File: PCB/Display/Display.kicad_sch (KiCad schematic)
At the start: 30 parts, among them J1 DC, J2 USB-C, M1 OLED1.5-RGB, U1 L86-M33, U2 ESP32-PICO-MINI-02, U3 FT231XQ, U4 LMR16006+FB, U5 QR

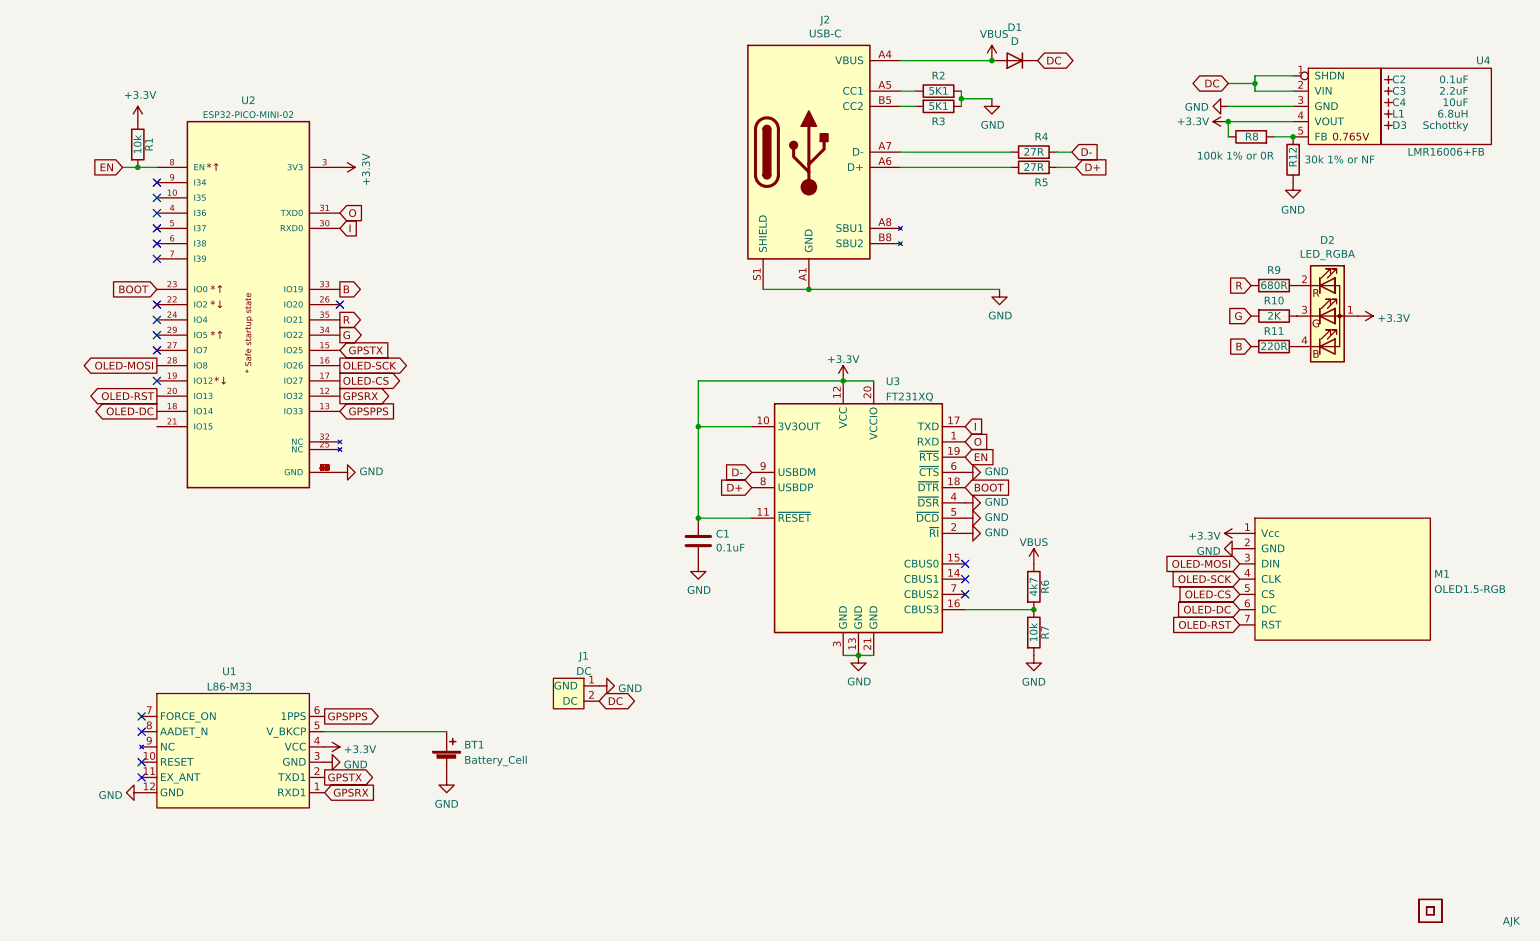
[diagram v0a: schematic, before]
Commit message: Started update on display.
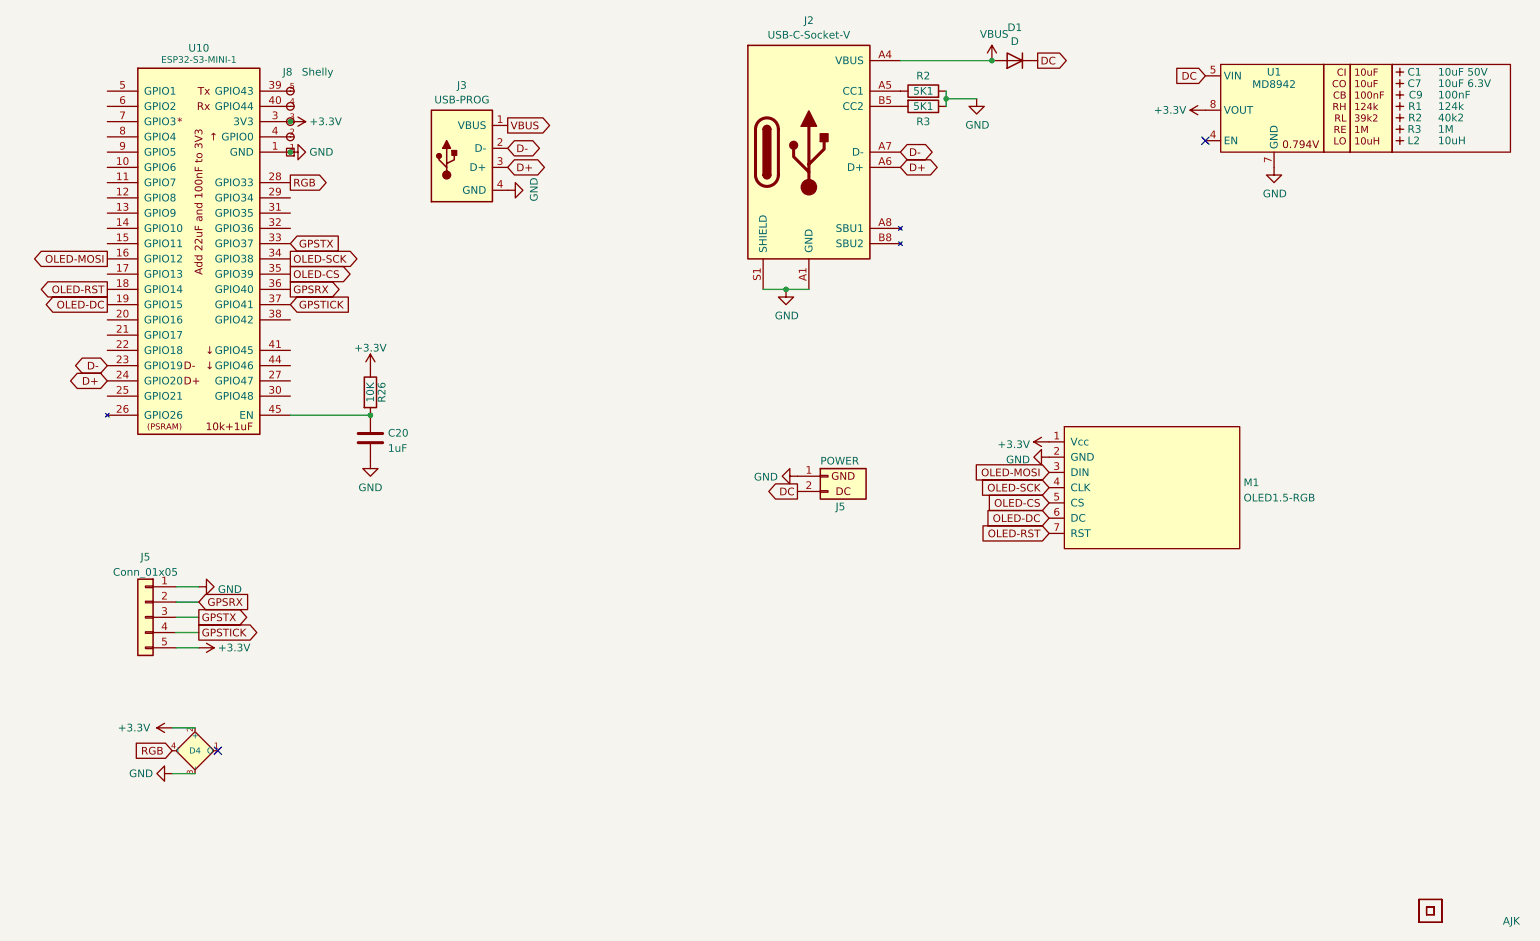
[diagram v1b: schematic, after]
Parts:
- removed BT1: Battery_Cell, RevK:Battery-Holder-2032, symbol Device:Battery_Cell
- removed C1: 0.1uF, RevK:C_0603, symbol Device:C
- removed C2: 0.1uF, RevK:Hidden, symbol RevK:Hidden
- removed C3: 2.2uF, RevK:Hidden, symbol RevK:Hidden
- removed C4: 10uF, RevK:Hidden, symbol RevK:Hidden
- removed D2: LED_RGBA, RevK:LED-RGB-1.6x1.6, symbol Device:LED_ARGB
- removed D3: Schottky, RevK:Hidden, symbol RevK:Hidden
- removed J1: DC, RevK:Molex_MiniSPOX_H2RA, symbol RevK:DC
- removed J2: USB-C, RevK:USC16-TR-Round, symbol RevK:USB-C
- removed L1: 6.8uH, RevK:Hidden, symbol RevK:Hidden
- removed R1, R7: 10k, RevK:R_0603, symbol Device:R
- removed R10: 2K, RevK:R_0603, symbol Device:R
- removed R11: 220R, RevK:R_0603, symbol Device:R
- removed R12: 30k 1% or NF, RevK:R_0603, symbol Device:R
- removed R4, R5: 27R, RevK:R_0603, symbol Device:R
- removed R6: 4k7, RevK:R_0603, symbol Device:R
- removed R8: 100k 1% or 0R, RevK:R_0603, symbol Device:R
- removed R9: 680R, RevK:R_0603, symbol Device:R
- removed U1: L86-M33, RevK:L86-M33, symbol RevK:L86-M33
- removed U2: ESP32-PICO-MINI-02, RevK:ESP32-PICO-MINI-02, symbol RevK:ESP32-PICO-MINI-02
- removed U3: FT231XQ, RevK:QFN-20-1EP_4x4mm_P0.5mm_EP2.5x2.5mm, symbol RevK:FT231XQ
- removed U4: LMR16006+FB, RevK:RegulatorBlockFB, symbol RevK:LMR16006+FB
- added C1: 10uF 50V, RevK:C_0603_, symbol RevK:Hidden
- added C20: 1uF, RevK:C_0402, symbol Device:C
- added C7: 10uF 6.3V, RevK:C_0603_, symbol RevK:Hidden
- added C9: 100nF, RevK:C_0603_, symbol RevK:Hidden
- added D4: XL-1010RGBC-WS2812B, RevK:SMD1010, symbol RevK:WS2812B-1mm
- added J2: USB-C-Socket-V, RevK:USB-C-Socket-H, symbol RevK:USB-C-Socket-H
- added J3: USB-PROG, RevK:USB-PROG, symbol RevK:USB-PROG
- added J5: POWER, RevK:PTSM-HH1-2-RA, symbol RevK:PowerIn
- added J5: Conn_01x05, RevK:PTSM-HH-5-RA-SMD, symbol Connector_Generic:Conn_01x05
- added J8: Shelly, RevK:Shelly, symbol RevK:Shelly
- added L2: 10uH, RevK:L_4x4_, symbol RevK:Hidden
- added R1: 124k, RevK:R_0402_, symbol RevK:Hidden
- added R2: 40k2, RevK:R_0402_, symbol RevK:Hidden
- added R26: 10K, RevK:R_0402, symbol Device:R
- added R3: 1M, RevK:R_0402_, symbol RevK:Hidden
- added U1: MD8942, RevK:SOT-23-6-MD8942, symbol RevK:MD89420-RegBlock
- added U10: ESP32-S3-MINI-1, RevK:ESP32-S3-MINI-1, symbol RevK:ESP32-S3-MINI-1-N4R2
- R2, R3: footprint RevK:R_0603 -> RevK:R_0402
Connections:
- net +3V3: now also D4.2 (+), J5.5 (Pin_5), J8.3 (3V3), R26.1, U1.8 (VOUT), U10.3 (3V3)
- net D+: now also J2.A6 (D+), J2.B6 (D+), J3.3 (D+), U10.24 (GPIO20)
- net D-: now also J2.A7 (D-), J2.B7 (D-), J3.2 (D-), U10.23 (GPIO19)
- net DC: now also J5.2 (DC), U1.5 (VIN)
- net GND: now also C20.2, D4.3 (-), J2.A1 (GND), J2.A12 (GND), J2.B1 (GND), J2.B12 (GND), J2.S1 (SHIELD), J3.4 (GND), J5.1 (GND), J5.1 (Pin_1), J8.1 (GND), U1.2 (GND), U1.7 (GND), U10.1 (GND), U10.2 (GND), U10.42 (GND), U10.43 (GND), U10.46 (GND), U10.47 (GND), U10.48 (GND), U10.49 (GND), U10.50 (GND), U10.51 (GND), U10.52 (GND), U10.53 (GND), U10.54 (GND), U10.55 (GND), U10.56 (GND), U10.57 (GND), U10.58 (GND), U10.59 (GND), U10.60 (GND), U10.61 (GND), U10.62 (GND), U10.63 (GND), U10.64 (GND), U10.65 (GND)
- net GPSRX: now also J5.2 (Pin_2), U10.36 (GPIO40)
- net GPSTX: now also J5.3 (Pin_3), U10.33 (GPIO37)
- net OLED-CS: now also U10.35 (GPIO39)
- net OLED-DC: now also U10.19 (GPIO15)
- net OLED-MOSI: now also U10.16 (GPIO12)
- net OLED-RST: now also U10.18 (GPIO14)
- net OLED-SCK: now also U10.34 (GPIO38)
- net VBUS: now also J2.A4 (VBUS), J2.A9 (VBUS), J2.B4 (VBUS), J2.B9 (VBUS), J3.1 (VBUS)
- net at R2.1: now also J2.A5 (CC1)
- net at R3.2: now also J2.B5 (CC2)
- new net: J8.5 (Tx), U10.39 (GPIO43)
- new net: J8.2 (0), U10.4 (GPIO0)
- new net: J8.4 (Rx), U10.40 (GPIO44)
- new net: C20.1, R26.2, U10.45 (EN)
- new net GPSTICK: J5.4 (Pin_4), U10.37 (GPIO41)
- new net RGB: D4.4 (I), U10.28 (GPIO33)
- no-connect marks 19 -> 2
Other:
- moved on the sheet: M1, R2, R3

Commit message: SD
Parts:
- added J6: DM3AT-SF-PEJM5, Connector_Card:microSD_HC_Hirose_DM3AT-SF-PEJM5, symbol Connector:Micro_SD_Card
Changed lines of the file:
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@@
+    )
+  )
+  (symbol (lib_id "Connector:Micro_SD_Card") (at 143.51 132.715 0) (unit 1)
+    (in_bom yes) (on_board yes) (dnp no) (fields_autoplaced)
+    (property "Reference" "J6" (at 144.145 114.6007 0)
+      (effects (font (size 1.27 1.27)))
+    )
+    (property "Value" "DM3AT-SF-PEJM5" (at 144.145 117.0249 0)
+      (effects (font (size 1.27 1.27)))
+    )
+    (property "Footprint" "Connector_Card:microSD_HC_Hirose_DM3AT-SF-PEJM5" (at 172.72 125.095 0)
+      (effects (font (size 1.27 1.27)) hide)
+    )
+    (property "Datasheet" "http://katalog.we-online.de/em/datasheet/693072010801.pdf" (at 143.51 132.715 0)
+      (effects (font (size 1.27 1.27)) hide)
+    )
+    (pin "5")
+    (pin "6")
+    (pin "1")
+    (pin "9")
+    (pin "2")
+    (pin "3")
+    (pin "4")
+    (pin "7")
+    (pin "8")
+    (instances
+      (project "Display"
+        (path "/babeabf2-f3b0-4ed5-8d9e-0215947e6cf3"
+          (reference "J6") (unit 1)
+        )
+      )
     )
   )

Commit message: PCB Update
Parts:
- C1: LCSC Part # C1591 -> (none); MPN (none) -> C1591
- C7: LCSC Part # C1691 -> (none); MPN (none) -> C1691
- D4: LCSC Part # C5349953 -> (none); MPN (none) -> C5349953
- J2: LCSC Part # C709357 -> (none); MPN (none) -> C709357
- U1: LCSC Part # C2684786 -> (none); MPN (none) -> C2684786
- U10: LCSC Part # C3013941 -> (none); MPN (none) -> C3013941
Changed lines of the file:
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@@
       (effects (font (size 1.27 1.27)) hide)
     )
-    (property "LCSC Part #" "C1591" (at 257.81 32.385 0)
+    (property "MPN" "C1591" (at 257.81 32.385 0)
       (effects (font (size 1.27 1.27)) hide)
     )
@@
       (effects (font (size 1 1)) (justify left top) hide)
     )
-    (property "LCSC Part #" "C5349953" (at 58.42 133.985 0)
+    (property "MPN" "C5349953" (at 58.42 133.985 0)
       (effects (font (size 1 1)) (justify left top) hide)
     )
@@
       (effects (font (size 1.27 1.27)) (justify left bottom) hide)
     )
-    (property "LCSC Part #" "C3013941" (at 57.785 94.615 0)
+    (property "MPN" "C3013941" (at 57.785 94.615 0)
       (effects (font (size 1.27 1.27)) hide)
     )
@@
       (effects (font (size 1.27 1.27)) hide)
     )
-    (property "LCSC Part #" "C709357" (at 159.385 45.72 0)
+    (property "MPN" "C709357" (at 159.385 45.72 0)
       (effects (font (size 1.27 1.27)) hide)
     )
@@
       (effects (font (size 1.27 1.27)) hide)
     )
-    (property "LCSC Part #" "C1691" (at 257.81 34.29 0)
+    (property "MPN" "C1691" (at 257.81 34.29 0)
       (effects (font (size 1.27 1.27)) hide)
     )
@@
       (effects (font (size 1.27 1.27)) hide)
     )
-    (property "LCSC Part #" "C2684786" (at 236.855 65.405 0)
-      (effects (font (size 1.27 1.27)) hide)
-    )
+    (property "MPN" "C2684786" (at 236.855 65.405 0)
+      (effects (font (size 1.27 1.27)) hide)
+    )
